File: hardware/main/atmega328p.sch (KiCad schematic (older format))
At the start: 17 parts, among them J401 USART, U401 ATMEGA328P-PU, Y401 16MHz

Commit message: Abstração do esquemático modificada para separar as duas placas e mostrar a conexão entre elas na folha principal
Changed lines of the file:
@@
 EESchema Schematic File Version 4
 LIBS:main-cache
-EELAYER 26 0
+EELAYER 29 0
 EELAYER END
 $Descr A4 11693 8268
 encoding utf-8
-Sheet 3 8
+Sheet 3 9
 Title ""
 Date ""
@@
 U 1 1 59FE3A5A
 P 8300 3600
-F 0 "Y401" H 8300 3700 50  0000 C CNN
+F 0 "Y?" H 8300 3700 50  0000 C CNN
 F 1 "16MHz" H 8300 3500 50  0000 C CNN
 F 2 "Crystal:Crystal_HC49-U_Vertical" H 8300 3600 50  0001 C CNN
@@
 U 1 1 59FE3A61
 P 8050 3800
-F 0 "C403" H 8060 3870 50  0000 L CNN
+F 0 "C?" H 8060 3870 50  0000 L CNN
 F 1 "22pF" H 8060 3720 50  0000 L CNN
 F 2 "Capacitor_SMD:C_0805_2012Metric_Pad1.15x1.40mm_HandSolder" H 8050 3800 50  0001 C CNN
@@
 U 1 1 59FE3A68
 P 8550 3800
-F 0 "C404" H 8350 3900 50  0000 L CNN
+F 0 "C?" H 8350 3900 50  0000 L CNN
 F 1 "22pF" H 8350 3700 50  0000 L CNN
 F 2 "Capacitor_SMD:C_0805_2012Metric_Pad1.15x1.40mm_HandSolder" H 8550 3800 50  0001 C CNN
@@
 U 1 1 59FE4B17
 P 6150 4050
-F 0 "R401" H 6180 4070 50  0000 L CNN
+F 0 "R?" H 6180 4070 50  0000 L CNN
 F 1 "10k" H 6180 4010 50  0000 L CNN
 F 2 "Resistor_SMD:R_0805_2012Metric_Pad1.15x1.40mm_HandSolder" H 6150 4050 50  0001 C CNN
@@
 U 1 1 59FE4EE2
 P 6000 4350
-F 0 "C406" V 5900 4250 50  0000 L CNN
+F 0 "C?" V 5900 4250 50  0000 L CNN
 F 1 "100nF" V 6050 4400 50  0000 L CNN
 F 2 "Capacitor_SMD:C_0805_2012Metric_Pad1.15x1.40mm_HandSolder" H 6000 4350 50  0001 C CNN
@@
 U 1 1 59FE5354
 P 5900 5500
-F 0 "D402" H 5850 5625 50  0000 L CNN
+F 0 "D?" H 5850 5625 50  0000 L CNN
 F 1 "LED_RED" H 5800 5400 50  0000 L CNN
 F 2 "LED_SMD:LED_0805_2012Metric_Pad1.15x1.40mm_HandSolder" V 5900 5500 50  0001 C CNN
@@
 U 1 1 59FFC489
 P 5900 5200
-F 0 "R404" H 5930 5220 50  0000 L CNN
+F 0 "R?" H 5930 5220 50  0000 L CNN
 F 1 "1k" H 5930 5160 50  0000 L CNN
 F 2 "Resistor_SMD:R_0805_2012Metric_Pad1.15x1.40mm_HandSolder" H 5900 5200 50  0001 C CNN
@@
 U 1 1 59FE3414
 P 4350 3950
-F 0 "U401" H 3850 5400 50  0000 L BNN
+F 0 "U?" H 3850 5400 50  0000 L BNN
 F 1 "ATMEGA328P-PU" H 4500 2450 50  0000 L BNN
 F 2 "Package_DIP:DIP-28_W7.62mm_Socket" H 4350 3950 50  0001 C CIN
@@
 U 1 1 5AACAE36
 P 7350 4350
-F 0 "R402" V 7400 4450 50  0000 L CNN
+F 0 "R?" V 7400 4450 50  0000 L CNN
 F 1 "1k" V 7400 4200 50  0000 L CNN
 F 2 "Resistor_SMD:R_0805_2012Metric_Pad1.15x1.40mm_HandSolder" H 7350 4350 50  0001 C CNN
@@
 U 1 1 5AACB0BA
 P 7350 4450
-F 0 "R403" V 7400 4550 50  0000 L CNN
+F 0 "R?" V 7400 4550 50  0000 L CNN
 F 1 "1k" V 7400 4300 50  0000 L CNN
 F 2 "Resistor_SMD:R_0805_2012Metric_Pad1.15x1.40mm_HandSolder" H 7350 4450 50  0001 C CNN
@@
 U 1 1 5BE7DD75
 P 6200 5500
-F 0 "D403" H 6150 5625 50  0000 L CNN
+F 0 "D?" H 6150 5625 50  0000 L CNN
 F 1 "LED_RED" H 6100 5400 50  0000 L CNN
 F 2 "LED_SMD:LED_0805_2012Metric_Pad1.15x1.40mm_HandSolder" V 6200 5500 50  0001 C CNN
@@
 U 1 1 5BE7DD7B
 P 6200 5200
-F 0 "R405" H 6230 5220 50  0000 L CNN
+F 0 "R?" H 6230 5220 50  0000 L CNN
 F 1 "1k" H 6230 5160 50  0000 L CNN
 F 2 "Resistor_SMD:R_0805_2012Metric_Pad1.15x1.40mm_HandSolder" H 6200 5200 50  0001 C CNN
@@
 U 1 1 5BE95CC8
 P 5900 4050
-F 0 "D401" V 5800 4200 50  0000 R CNN
+F 0 "D?" V 5800 4200 50  0000 R CNN
 F 1 "LL4148" V 5900 4350 50  0000 R CNN
 F 2 "Diode_SMD:D_MiniMELF_Handsoldering" H 5900 3875 50  0001 C CNN
@@
 U 1 1 5BEB6AE8
 P 8300 4100
-F 0 "#PWR0407" H 8300 3850 50  0001 C CNN
+F 0 "#PWR?" H 8300 3850 50  0001 C CNN
 F 1 "GND" H 8350 3900 50  0000 C CNN
 F 2 "" H 8300 4100 50  0001 C CNN
@@
 U 1 1 5BEB7AB4
 P 4350 5750
-F 0 "#PWR0412" H 4350 5500 50  0001 C CNN
+F 0 "#PWR?" H 4350 5500 50  0001 C CNN
 F 1 "GND" H 4400 5550 50  0000 C CNN
 F 2 "" H 4350 5750 50  0001 C CNN
@@
 U 1 1 5BEC895B
 P 8050 2450
-F 0 "#PWR0404" H 8050 2200 50  0001 C CNN
+F 0 "#PWR?" H 8050 2200 50  0001 C CNN
 F 1 "GND" H 8100 2250 50  0000 C CNN
 F 2 "" H 8050 2450 50  0001 C CNN
@@
 U 1 1 5BECD3FE
 P 7750 4450
-F 0 "J401" H 7700 4000 50  0000 C CNN
+F 0 "J?" H 7700 4000 50  0000 C CNN
 F 1 "USART" H 7700 4100 50  0000 C CNN
 F 2 "Connector_PinHeader_2.54mm:PinHeader_1x04_P2.54mm_Vertical" H 7750 4450 50  0001 C CNN
@@
 U 1 1 5BECF494
 P 5750 4400
-F 0 "#PWR0408" H 5750 4150 50  0001 C CNN
+F 0 "#PWR?" H 5750 4150 50  0001 C CNN
 F 1 "GND" H 5650 4400 50  0000 C CNN
 F 2 "" H 5750 4400 50  0001 C CNN
@@
 U 1 1 5BED8033
 P 6300 4250
-F 0 "C405" V 6200 4100 50  0000 L CNN
+F 0 "C?" V 6200 4100 50  0000 L CNN
 F 1 "100nF" V 6100 4000 50  0000 L CNN
 F 2 "Capacitor_SMD:C_0805_2012Metric_Pad1.15x1.40mm_HandSolder" H 6300 4250 50  0001 C CNN
@@
 U 1 1 5BEE0905
 P 7450 4650
-F 0 "#PWR0409" H 7450 4400 50  0001 C CNN
+F 0 "#PWR?" H 7450 4400 50  0001 C CNN
 F 1 "GND" H 7500 4450 50  0000 C CNN
 F 2 "" H 7450 4650 50  0001 C CNN
@@
 U 1 1 5BF321D4
 P 4350 1750
-F 0 "#PWR0401" H 4350 1600 50  0001 C CNN
+F 0 "#PWR?" H 4350 1600 50  0001 C CNN
 F 1 "+5V" H 4400 1950 50  0000 C CNN
 F 2 "" H 4350 1750 50  0001 C CNN
@@
 U 1 1 5BF32222
 P 8050 2150
-F 0 "#PWR0402" H 8050 2000 50  0001 C CNN
+F 0 "#PWR?" H 8050 2000 50  0001 C CNN
 F 1 "+5V" H 8100 2350 50  0000 C CNN
 F 2 "" H 8050 2150 50  0001 C CNN
@@
 U 1 1 5BF330B7
 P 5900 3750
-F 0 "#PWR0406" H 5900 3600 50  0001 C CNN
+F 0 "#PWR?" H 5900 3600 50  0001 C CNN
 F 1 "+5V" H 5950 3950 50  0000 C CNN
 F 2 "" H 5900 3750 50  0001 C CNN
@@
 U 1 1 5BF3B4C1
 P 3650 2950
-F 0 "C402" H 3700 2850 50  0000 L CNN
+F 0 "C?" H 3700 2850 50  0000 L CNN
 F 1 "100nF" H 3700 3050 50  0000 L CNN
 F 2 "Capacitor_SMD:C_0805_2012Metric_Pad1.15x1.40mm_HandSolder" H 3650 2950 50  0001 C CNN
@@
 U 1 1 5BF3D2B5
 P 3650 3150
-F 0 "#PWR0405" H 3650 2900 50  0001 C CNN
+F 0 "#PWR?" H 3650 2900 50  0001 C CNN
 F 1 "GND" H 3700 2950 50  0000 C CNN
 F 2 "" H 3650 3150 50  0001 C CNN
@@
 U 1 1 5BF2780D
 P 4550 2050
-F 0 "C401" H 4650 2050 50  0000 L CNN
+F 0 "C?" H 4650 2050 50  0000 L CNN
 F 1 "100nF" H 4550 2150 50  0000 L CNN
 F 2 "Capacitor_SMD:C_0805_2012Metric_Pad1.15x1.40mm_HandSolder" H 4550 2050 50  0001 C CNN
@@
 U 1 1 5BF3B38D
 P 4550 2250
-F 0 "#PWR0403" H 4550 2000 50  0001 C CNN
+F 0 "#PWR?" H 4550 2000 50  0001 C CNN
 F 1 "GND" H 4600 2050 50  0000 C CNN
 F 2 "" H 4550 2250 50  0001 C CNN

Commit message: TO-DO List criada na folha principal
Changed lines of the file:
@@
 $Descr A4 11693 8268
 encoding utf-8
-Sheet 3 9
+Sheet 5 9
 Title ""
 Date ""
@@
 U 1 1 59FE3A5A
 P 8300 3600
-F 0 "Y?" H 8300 3700 50  0000 C CNN
+AR Path="/5AACA401/59FE3A5A" Ref="Y401"  Part="1"
+AR Path="/5CA4DC1F/5CA5A5BB/59FE3A5A" Ref="Y501"  Part="1"
+F 0 "Y501" H 8300 3700 50  0000 C CNN
 F 1 "16MHz" H 8300 3500 50  0000 C CNN
 F 2 "Crystal:Crystal_HC49-U_Vertical" H 8300 3600 50  0001 C CNN
@@
 U 1 1 59FE3A61
 P 8050 3800
-F 0 "C?" H 8060 3870 50  0000 L CNN
+AR Path="/5AACA401/59FE3A61" Ref="C403"  Part="1"
+AR Path="/5CA4DC1F/5CA5A5BB/59FE3A61" Ref="C503"  Part="1"
+F 0 "C503" H 8060 3870 50  0000 L CNN
 F 1 "22pF" H 8060 3720 50  0000 L CNN
 F 2 "Capacitor_SMD:C_0805_2012Metric_Pad1.15x1.40mm_HandSolder" H 8050 3800 50  0001 C CNN
@@
 U 1 1 59FE3A68
 P 8550 3800
-F 0 "C?" H 8350 3900 50  0000 L CNN
+AR Path="/5AACA401/59FE3A68" Ref="C404"  Part="1"
+AR Path="/5CA4DC1F/5CA5A5BB/59FE3A68" Ref="C504"  Part="1"
+F 0 "C504" H 8350 3900 50  0000 L CNN
 F 1 "22pF" H 8350 3700 50  0000 L CNN
 F 2 "Capacitor_SMD:C_0805_2012Metric_Pad1.15x1.40mm_HandSolder" H 8550 3800 50  0001 C CNN
@@
 U 1 1 59FE4B17
 P 6150 4050
-F 0 "R?" H 6180 4070 50  0000 L CNN
+AR Path="/5AACA401/59FE4B17" Ref="R401"  Part="1"
+AR Path="/5CA4DC1F/5CA5A5BB/59FE4B17" Ref="R501"  Part="1"
+F 0 "R501" H 6180 4070 50  0000 L CNN
 F 1 "10k" H 6180 4010 50  0000 L CNN
 F 2 "Resistor_SMD:R_0805_2012Metric_Pad1.15x1.40mm_HandSolder" H 6150 4050 50  0001 C CNN
@@
 U 1 1 59FE4EE2
 P 6000 4350
-F 0 "C?" V 5900 4250 50  0000 L CNN
+AR Path="/5AACA401/59FE4EE2" Ref="C406"  Part="1"
+AR Path="/5CA4DC1F/5CA5A5BB/59FE4EE2" Ref="C506"  Part="1"
+F 0 "C506" V 5900 4250 50  0000 L CNN
 F 1 "100nF" V 6050 4400 50  0000 L CNN
 F 2 "Capacitor_SMD:C_0805_2012Metric_Pad1.15x1.40mm_HandSolder" H 6000 4350 50  0001 C CNN
@@
 U 1 1 59FE5354
 P 5900 5500
-F 0 "D?" H 5850 5625 50  0000 L CNN
+AR Path="/5AACA401/59FE5354" Ref="D402"  Part="1"
+AR Path="/5CA4DC1F/5CA5A5BB/59FE5354" Ref="D502"  Part="1"
+F 0 "D502" H 5850 5625 50  0000 L CNN
 F 1 "LED_RED" H 5800 5400 50  0000 L CNN
 F 2 "LED_SMD:LED_0805_2012Metric_Pad1.15x1.40mm_HandSolder" V 5900 5500 50  0001 C CNN
@@
 U 1 1 59FFC489
 P 5900 5200
-F 0 "R?" H 5930 5220 50  0000 L CNN
+AR Path="/5AACA401/59FFC489" Ref="R404"  Part="1"
+AR Path="/5CA4DC1F/5CA5A5BB/59FFC489" Ref="R504"  Part="1"
+F 0 "R504" H 5930 5220 50  0000 L CNN
 F 1 "1k" H 5930 5160 50  0000 L CNN
 F 2 "Resistor_SMD:R_0805_2012Metric_Pad1.15x1.40mm_HandSolder" H 5900 5200 50  0001 C CNN
@@
 U 1 1 59FE3414
 P 4350 3950
-F 0 "U?" H 3850 5400 50  0000 L BNN
+AR Path="/5AACA401/59FE3414" Ref="U401"  Part="1"
+AR Path="/5CA4DC1F/5CA5A5BB/59FE3414" Ref="U501"  Part="1"
+F 0 "U501" H 3850 5400 50  0000 L BNN
 F 1 "ATMEGA328P-PU" H 4500 2450 50  0000 L BNN
 F 2 "Package_DIP:DIP-28_W7.62mm_Socket" H 4350 3950 50  0001 C CIN
@@
 U 1 1 5AACAE36
 P 7350 4350
-F 0 "R?" V 7400 4450 50  0000 L CNN
+AR Path="/5AACA401/5AACAE36" Ref="R402"  Part="1"
+AR Path="/5CA4DC1F/5CA5A5BB/5AACAE36" Ref="R502"  Part="1"
+F 0 "R502" V 7400 4450 50  0000 L CNN
 F 1 "1k" V 7400 4200 50  0000 L CNN
 F 2 "Resistor_SMD:R_0805_2012Metric_Pad1.15x1.40mm_HandSolder" H 7350 4350 50  0001 C CNN
@@
 U 1 1 5AACB0BA
 P 7350 4450
-F 0 "R?" V 7400 4550 50  0000 L CNN
+AR Path="/5AACA401/5AACB0BA" Ref="R403"  Part="1"
+AR Path="/5CA4DC1F/5CA5A5BB/5AACB0BA" Ref="R503"  Part="1"
+F 0 "R503" V 7400 4550 50  0000 L CNN
 F 1 "1k" V 7400 4300 50  0000 L CNN
 F 2 "Resistor_SMD:R_0805_2012Metric_Pad1.15x1.40mm_HandSolder" H 7350 4450 50  0001 C CNN
@@
 U 1 1 5BE7DD75
 P 6200 5500
-F 0 "D?" H 6150 5625 50  0000 L CNN
+AR Path="/5AACA401/5BE7DD75" Ref="D403"  Part="1"
+AR Path="/5CA4DC1F/5CA5A5BB/5BE7DD75" Ref="D503"  Part="1"
+F 0 "D503" H 6150 5625 50  0000 L CNN
 F 1 "LED_RED" H 6100 5400 50  0000 L CNN
 F 2 "LED_SMD:LED_0805_2012Metric_Pad1.15x1.40mm_HandSolder" V 6200 5500 50  0001 C CNN
@@
 U 1 1 5BE7DD7B
 P 6200 5200
-F 0 "R?" H 6230 5220 50  0000 L CNN
+AR Path="/5AACA401/5BE7DD7B" Ref="R405"  Part="1"
+AR Path="/5CA4DC1F/5CA5A5BB/5BE7DD7B" Ref="R505"  Part="1"
+F 0 "R505" H 6230 5220 50  0000 L CNN
 F 1 "1k" H 6230 5160 50  0000 L CNN
 F 2 "Resistor_SMD:R_0805_2012Metric_Pad1.15x1.40mm_HandSolder" H 6200 5200 50  0001 C CNN
@@
 U 1 1 5BE95CC8
 P 5900 4050
-F 0 "D?" V 5800 4200 50  0000 R CNN
+AR Path="/5AACA401/5BE95CC8" Ref="D401"  Part="1"
+AR Path="/5CA4DC1F/5CA5A5BB/5BE95CC8" Ref="D501"  Part="1"
+F 0 "D501" V 5800 4200 50  0000 R CNN
 F 1 "LL4148" V 5900 4350 50  0000 R CNN
 F 2 "Diode_SMD:D_MiniMELF_Handsoldering" H 5900 3875 50  0001 C CNN
@@
 U 1 1 5BEB6AE8
 P 8300 4100
-F 0 "#PWR?" H 8300 3850 50  0001 C CNN
+AR Path="/5AACA401/5BEB6AE8" Ref="#PWR0407"  Part="1"
+AR Path="/5CA4DC1F/5CA5A5BB/5BEB6AE8" Ref="#PWR0127"  Part="1"
+F 0 "#PWR0127" H 8300 3850 50  0001 C CNN
 F 1 "GND" H 8350 3900 50  0000 C CNN
 F 2 "" H 8300 4100 50  0001 C CNN
@@
 U 1 1 5BEB7AB4
 P 4350 5750
-F 0 "#PWR?" H 4350 5500 50  0001 C CNN
+AR Path="/5AACA401/5BEB7AB4" Ref="#PWR0412"  Part="1"
+AR Path="/5CA4DC1F/5CA5A5BB/5BEB7AB4" Ref="#PWR0128"  Part="1"
+F 0 "#PWR0128" H 4350 5500 50  0001 C CNN
 F 1 "GND" H 4400 5550 50  0000 C CNN
 F 2 "" H 4350 5750 50  0001 C CNN
@@
 U 1 1 5BEC895B
 P 8050 2450
-F 0 "#PWR?" H 8050 2200 50  0001 C CNN
+AR Path="/5AACA401/5BEC895B" Ref="#PWR0404"  Part="1"
+AR Path="/5CA4DC1F/5CA5A5BB/5BEC895B" Ref="#PWR0129"  Part="1"
+F 0 "#PWR0129" H 8050 2200 50  0001 C CNN
 F 1 "GND" H 8100 2250 50  0000 C CNN
 F 2 "" H 8050 2450 50  0001 C CNN
@@
 U 1 1 5BECD3FE
 P 7750 4450
-F 0 "J?" H 7700 4000 50  0000 C CNN
+AR Path="/5AACA401/5BECD3FE" Ref="J401"  Part="1"
+AR Path="/5CA4DC1F/5CA5A5BB/5BECD3FE" Ref="J501"  Part="1"
+F 0 "J501" H 7700 4000 50  0000 C CNN
 F 1 "USART" H 7700 4100 50  0000 C CNN
 F 2 "Connector_PinHeader_2.54mm:PinHeader_1x04_P2.54mm_Vertical" H 7750 4450 50  0001 C CNN
@@
 U 1 1 5BECF494
 P 5750 4400
-F 0 "#PWR?" H 5750 4150 50  0001 C CNN
+AR Path="/5AACA401/5BECF494" Ref="#PWR0408"  Part="1"
+AR Path="/5CA4DC1F/5CA5A5BB/5BECF494" Ref="#PWR0130"  Part="1"
+F 0 "#PWR0130" H 5750 4150 50  0001 C CNN
 F 1 "GND" H 5650 4400 50  0000 C CNN
 F 2 "" H 5750 4400 50  0001 C CNN
@@
 U 1 1 5BED8033
 P 6300 4250
-F 0 "C?" V 6200 4100 50  0000 L CNN
+AR Path="/5AACA401/5BED8033" Ref="C405"  Part="1"
+AR Path="/5CA4DC1F/5CA5A5BB/5BED8033" Ref="C505"  Part="1"
+F 0 "C505" V 6200 4100 50  0000 L CNN
 F 1 "100nF" V 6100 4000 50  0000 L CNN
 F 2 "Capacitor_SMD:C_0805_2012Metric_Pad1.15x1.40mm_HandSolder" H 6300 4250 50  0001 C CNN
@@
 U 1 1 5BEE0905
 P 7450 4650
-F 0 "#PWR?" H 7450 4400 50  0001 C CNN
+AR Path="/5AACA401/5BEE0905" Ref="#PWR0409"  Part="1"
+AR Path="/5CA4DC1F/5CA5A5BB/5BEE0905" Ref="#PWR0131"  Part="1"
+F 0 "#PWR0131" H 7450 4400 50  0001 C CNN
 F 1 "GND" H 7500 4450 50  0000 C CNN
 F 2 "" H 7450 4650 50  0001 C CNN
@@
 U 1 1 5BF321D4
 P 4350 1750
-F 0 "#PWR?" H 4350 1600 50  0001 C CNN
+AR Path="/5AACA401/5BF321D4" Ref="#PWR0401"  Part="1"
+AR Path="/5CA4DC1F/5CA5A5BB/5BF321D4" Ref="#PWR0132"  Part="1"
+F 0 "#PWR0132" H 4350 1600 50  0001 C CNN
 F 1 "+5V" H 4400 1950 50  0000 C CNN
 F 2 "" H 4350 1750 50  0001 C CNN
@@
 U 1 1 5BF32222
 P 8050 2150
-F 0 "#PWR?" H 8050 2000 50  0001 C CNN
+AR Path="/5AACA401/5BF32222" Ref="#PWR0402"  Part="1"
+AR Path="/5CA4DC1F/5CA5A5BB/5BF32222" Ref="#PWR0133"  Part="1"
+F 0 "#PWR0133" H 8050 2000 50  0001 C CNN
 F 1 "+5V" H 8100 2350 50  0000 C CNN
 F 2 "" H 8050 2150 50  0001 C CNN
@@
 U 1 1 5BF330B7
 P 5900 3750
-F 0 "#PWR?" H 5900 3600 50  0001 C CNN
+AR Path="/5AACA401/5BF330B7" Ref="#PWR0406"  Part="1"
+AR Path="/5CA4DC1F/5CA5A5BB/5BF330B7" Ref="#PWR0134"  Part="1"
+F 0 "#PWR0134" H 5900 3600 50  0001 C CNN
 F 1 "+5V" H 5950 3950 50  0000 C CNN
 F 2 "" H 5900 3750 50  0001 C CNN
@@
 U 1 1 5BF3B4C1
 P 3650 2950
-F 0 "C?" H 3700 2850 50  0000 L CNN
+AR Path="/5AACA401/5BF3B4C1" Ref="C402"  Part="1"
+AR Path="/5CA4DC1F/5CA5A5BB/5BF3B4C1" Ref="C502"  Part="1"
+F 0 "C502" H 3700 2850 50  0000 L CNN
 F 1 "100nF" H 3700 3050 50  0000 L CNN
 F 2 "Capacitor_SMD:C_0805_2012Metric_Pad1.15x1.40mm_HandSolder" H 3650 2950 50  0001 C CNN
@@
 U 1 1 5BF3D2B5
 P 3650 3150
-F 0 "#PWR?" H 3650 2900 50  0001 C CNN
+AR Path="/5AACA401/5BF3D2B5" Ref="#PWR0405"  Part="1"
+AR Path="/5CA4DC1F/5CA5A5BB/5BF3D2B5" Ref="#PWR0135"  Part="1"
+F 0 "#PWR0135" H 3650 2900 50  0001 C CNN
 F 1 "GND" H 3700 2950 50  0000 C CNN
 F 2 "" H 3650 3150 50  0001 C CNN
@@
 U 1 1 5BF2780D
 P 4550 2050
-F 0 "C?" H 4650 2050 50  0000 L CNN
+AR Path="/5AACA401/5BF2780D" Ref="C401"  Part="1"
+AR Path="/5CA4DC1F/5CA5A5BB/5BF2780D" Ref="C501"  Part="1"
+F 0 "C501" H 4650 2050 50  0000 L CNN
 F 1 "100nF" H 4550 2150 50  0000 L CNN
 F 2 "Capacitor_SMD:C_0805_2012Metric_Pad1.15x1.40mm_HandSolder" H 4550 2050 50  0001 C CNN
@@
 U 1 1 5BF3B38D
 P 4550 2250
-F 0 "#PWR?" H 4550 2000 50  0001 C CNN
+AR Path="/5AACA401/5BF3B38D" Ref="#PWR0403"  Part="1"
+AR Path="/5CA4DC1F/5CA5A5BB/5BF3B38D" Ref="#PWR0136"  Part="1"
+F 0 "#PWR0136" H 4550 2000 50  0001 C CNN
 F 1 "GND" H 4600 2050 50  0000 C CNN
 F 2 "" H 4550 2250 50  0001 C CNN

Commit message: CAN CTRL_D / CAN_ON_OFF removidos.
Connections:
- net CAN_CTRL: no longer names the net of U401.23 (PC0)
- no-connect marks 5 -> 6
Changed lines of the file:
@@
 $Descr A4 11693 8268
 encoding utf-8
-Sheet 5 9
+Sheet 5 8
 Title ""
 Date ""
@@
 Wire Wire Line
 	4550 2250 4550 2150
-Text HLabel 5250 3650 2    50   Output ~ 0
-CAN_CTRL
-Wire Wire Line
-	4950 3650 5250 3650
 Text HLabel 5250 3750 2    50   Output ~ 0
 RL_OFF
@@
 Wire Wire Line
 	4950 4150 5250 4150
+Wire Wire Line
+	4950 3650 5050 3650
+NoConn ~ 5050 3650
 $EndSCHEMATC

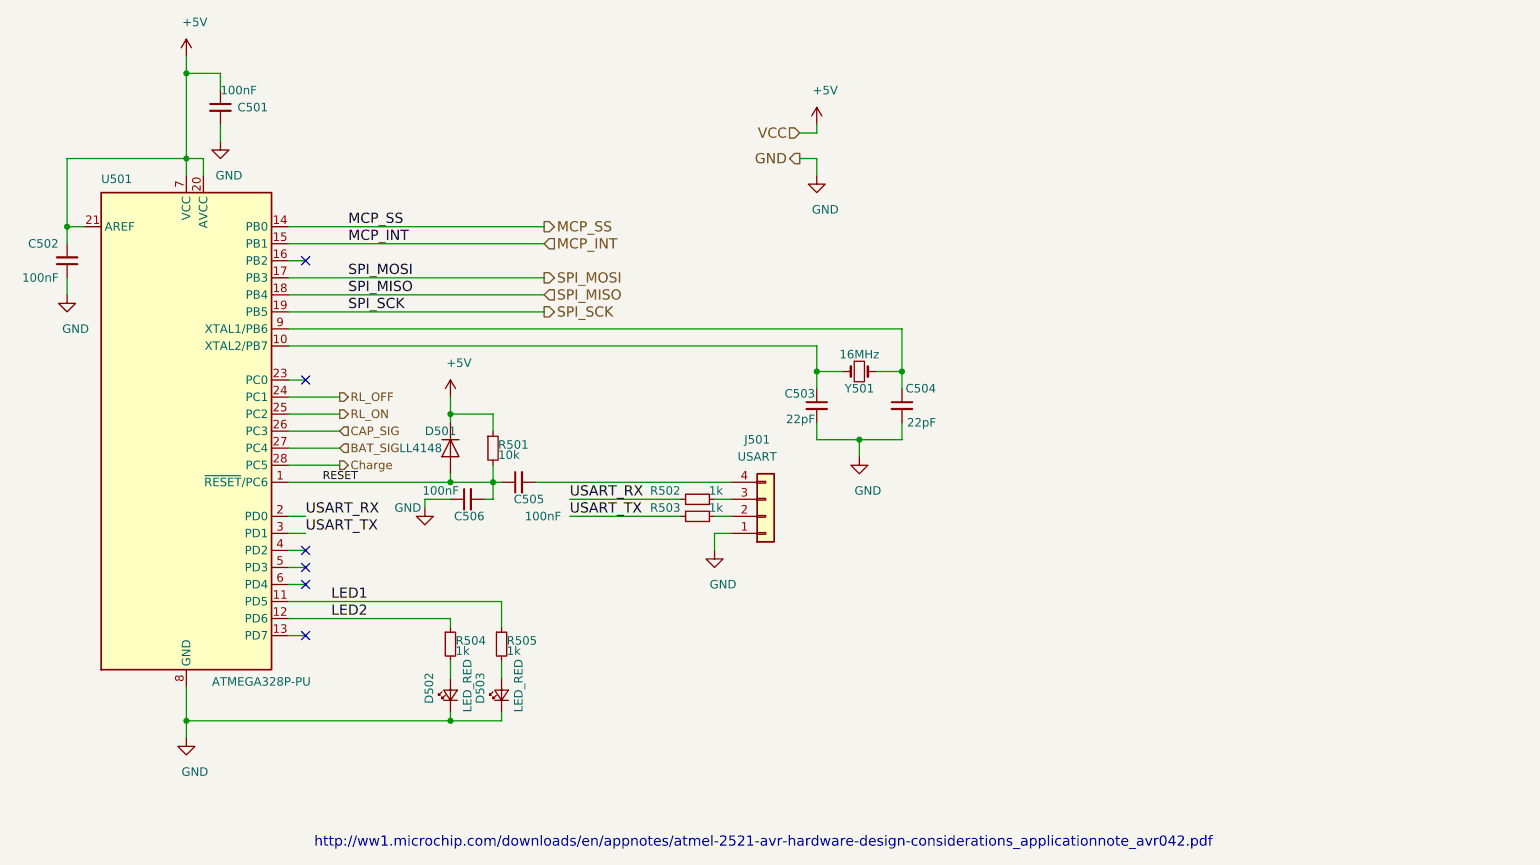
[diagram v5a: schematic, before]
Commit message: Esquematico primeira versão Erro de referencia dos componentes na PCB com os do Esquematico solucionados
Pontos de teste adicionados
Alimentar o analog com +12V
Adicionar Snubber para os reles
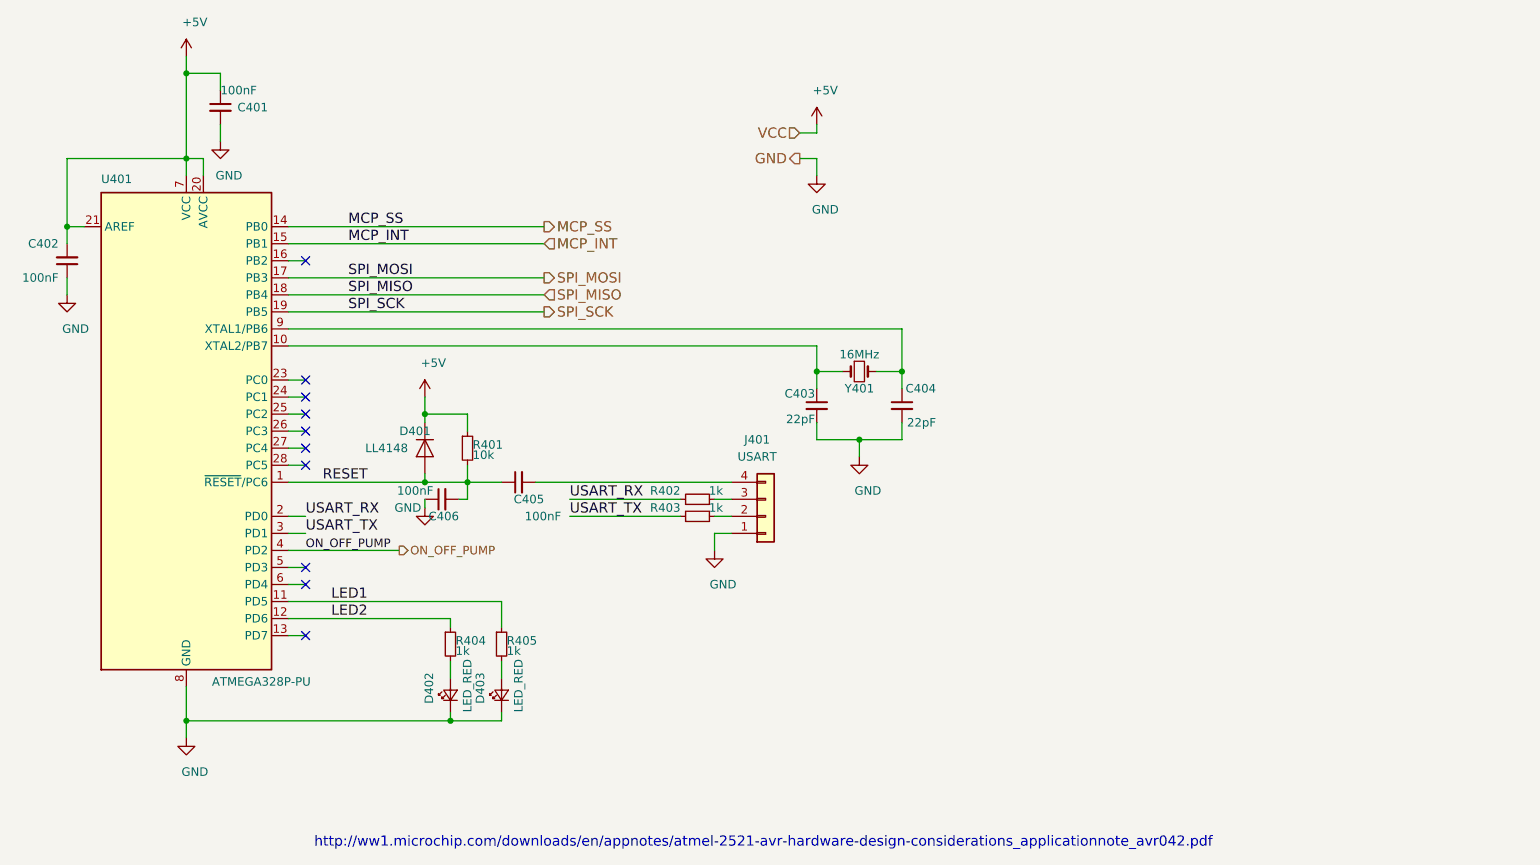
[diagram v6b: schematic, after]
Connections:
- net ON_OFF_PUMP: now reaches U401.4 (PD2)
- net BAT_SIG: no longer names the net of U401.27 (PC4)
- net CAP_SIG: no longer names the net of U401.26 (PC3)
- net Charge: no longer names the net of U401.28 (PC5)
- net RL_OFF: no longer names the net of U401.24 (PC1)
- net RL_ON: no longer names the net of U401.25 (PC2)
- no-connect marks 6 -> 10
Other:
- moved on the sheet: C406, D401, R401

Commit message: Footprints
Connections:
- net Charge: now reaches U401.23 (PC0)
- net RL_OFF: now reaches U401.24 (PC1)
- net RL_ON: now reaches U401.25 (PC2)
- net CAP_SIG: now reaches U401.26 (PC3)
- net BAT_SIG: now reaches U401.27 (PC4)
- net ON_OFF_PUMP: no longer names the net of U401.4 (PD2)
- no-connect marks 10 -> 6
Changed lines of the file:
@@
 	0    -1   -1   0
 $EndComp
-NoConn ~ 5050 3850
-NoConn ~ 5050 3950
-NoConn ~ 5050 4050
-NoConn ~ 5050 4150
 NoConn ~ 5050 4750
 NoConn ~ 5050 4850
@@
 Wire Wire Line
 	5900 5300 5900 5400
-NoConn ~ 5050 3750
 Wire Wire Line
 	4350 5450 4350 5650
@@
 Wire Wire Line
 	4550 2250 4550 2150
-NoConn ~ 5050 3650
 Wire Wire Line
 	5950 4350 6000 4350
-Text Label 5050 4650 0    50   ~ 0
-ON_OFF_PUMP
-Text HLabel 5600 4650 2    50   Output ~ 0
-ON_OFF_PUMP
-Wire Wire Line
-	4950 4650 5600 4650
+NoConn ~ 5050 4650
+Wire Wire Line
+	4950 4650 5050 4650
+Text HLabel 5050 3750 2    50   Input ~ 0
+RL_OFF
+Text HLabel 5050 3850 2    50   Input ~ 0
+RL_ON
+Text HLabel 5050 3950 2    50   Input ~ 0
+CAP_SIG
+Text HLabel 5050 4050 2    50   Input ~ 0
+BAT_SIG
+NoConn ~ 5050 4150
+Text HLabel 5050 3650 2    50   Input ~ 0
+Charge
 $EndSCHEMATC
